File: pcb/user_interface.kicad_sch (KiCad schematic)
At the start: 8 parts, among them SW3 GSPTS0018

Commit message: Finished user interface
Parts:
- added D5: B38G3RGB, B38G3RGB:B38G3RGB-10D0003H2U1930_HVK, symbol Device:LED_RGBA
- added Q6: NTR4003N, Package_TO_SOT_SMD:SOT-23-3, symbol Transistor_FET:Q_NMOS_GSD
- added R34: 430, Resistor_SMD:R_0603_1608Metric, symbol Device:R_Small_US
- added R35, R36: 330, Resistor_SMD:R_0603_1608Metric, symbol Device:R_Small_US
- added R37: 100, symbol Device:R_Small_US
- added R38: 47k, symbol Device:R_Small_US
- added SW4, SW5, SW6: GSPTS0018, PTS815_SJM_250_SMTR_LFS:SW_Push_PTS815_SJM_250_SMTR_LFS, symbol Switch:SW_Push
- R17: value 330 -> 430
- R32, R33: value 150 -> 330
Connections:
- net +3V3: now also BZ1.1 (+), D4.1 (K), SW3.2, SW4.2, SW5.2, SW6.2
- net +BATT: now also D5.4 (A)
- net BTN_0: now also SW3.1
- net BTN_1: now also SW4.1
- net BTN_2: now also SW5.1
- net BTN_3: now also SW6.1
- net MODE_1: now also S1.1
- net MODE_2: now also S1.2
- net MODE_4: now also S1.4
- net MODE_C: now also S1.C
- net at BZ1.2 (-): now also D4.2 (A), Q6.3 (D)
- new net: Q6.1 (G), R37.2, R38.1
- new net: D5.2 (GK), R35.1
- new net: D5.1 (RK), R34.1
- new net: D5.3 (BK), R36.1
- new net BUZZER: R37.1
- new net GND: Q6.2 (S), R38.2
- new net LED1_B: R36.2
- new net LED1_G: R35.2
- new net LED1_R: R34.2
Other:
- note added: "15 mA"
- note added: "red 2V green/blue 3.3V"
- note removed: "red 2V green/blue 3V"
- moved on the sheet: BZ1, D4

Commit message: Start layout
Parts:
- D4: footprint (none) -> Diode_SMD:D_SMA
- R33: renamed from R37; footprint (none) -> Resistor_SMD:R_0603_1608Metric
- R35: renamed from R38; footprint (none) -> Resistor_SMD:R_0603_1608Metric
- renumbered R17 to R32, R32 to R34, R33 to R36, R34 to R37, R35 to R38, R36 to R39
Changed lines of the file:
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@@
 		(on_board yes)
 		(dnp no)
-		(property "Reference" "R32"
+		(property "Reference" "R34"
 			(at 45.212 44.45 0)
 			(effects
@@
 			(project "airbrake_mod"
 				(path "/1f4fd4ed-9886-4375-a5ac-dc32d5760936/0a32b07f-7988-40ae-8006-b298a5ae2a50"
-					(reference "R32")
+					(reference "R34")
 					(unit 1)
 				)
@@
 		(dnp no)
 		(fields_autoplaced yes)
-		(property "Reference" "#PWR077"
+		(property "Reference" "#PWR067"
 			(at 158.75 80.01 0)
 			(effects
@@
 			(project "airbrake_mod"
 				(path "/1f4fd4ed-9886-4375-a5ac-dc32d5760936/0a32b07f-7988-40ae-8006-b298a5ae2a50"
-					(reference "#PWR077")
+					(reference "#PWR067")
 					(unit 1)
 				)
@@
 			)
 		)
-		(property "Footprint" ""
+		(property "Footprint" "Diode_SMD:D_SMA"
 			(at 60.96 133.35 90)
 			(effects
@@
 		(dnp no)
 		(fields_autoplaced yes)
-		(property "Reference" "#PWR081"
+		(property "Reference" "#PWR062"
 			(at 63.5 171.45 0)
 			(effects
@@
 			(project "airbrake_mod"
 				(path "/1f4fd4ed-9886-4375-a5ac-dc32d5760936/0a32b07f-7988-40ae-8006-b298a5ae2a50"
-					(reference "#PWR081")
+					(reference "#PWR062")
 					(unit 1)
 				)
@@
 		(dnp no)
 		(fields_autoplaced yes)
-		(property "Reference" "#PWR069"
+		(property "Reference" "#PWR061"
 			(at 63.5 130.81 0)
 			(effects
@@
 			(project ""
 				(path "/1f4fd4ed-9886-4375-a5ac-dc32d5760936/0a32b07f-7988-40ae-8006-b298a5ae2a50"
-					(reference "#PWR069")
+					(reference "#PWR061")
 					(unit 1)
 				)
@@
 		(dnp no)
 		(fields_autoplaced yes)
-		(property "Reference" "R38"
+		(property "Reference" "R35"
 			(at 53.34 157.4799 0)
 			(effects
@@
 			)
 		)
-		(property "Footprint" ""
+		(property "Footprint" "Resistor_SMD:R_0603_1608Metric"
 			(at 50.8 158.75 0)
 			(effects
@@
 			(project "airbrake_mod"
 				(path "/1f4fd4ed-9886-4375-a5ac-dc32d5760936/0a32b07f-7988-40ae-8006-b298a5ae2a50"
-					(reference "R38")
+					(reference "R35")
 					(unit 1)
 				)
@@
 		(dnp no)
 		(fields_autoplaced yes)
-		(property "Reference" "#PWR080"
+		(property "Reference" "#PWR060"
 			(at 50.8 171.45 0)
 			(effects
@@
 			(project "airbrake_mod"
 				(path "/1f4fd4ed-9886-4375-a5ac-dc32d5760936/0a32b07f-7988-40ae-8006-b298a5ae2a50"
-					(reference "#PWR080")
+					(reference "#PWR060")
 					(unit 1)
 				)
@@
 		(dnp no)
 		(fields_autoplaced yes)
-		(property "Reference" "#PWR075"
+		(property "Reference" "#PWR064"
 			(at 120.65 80.01 0)
 			(effects
@@
 			(project "airbrake_mod"
 				(path "/1f4fd4ed-9886-4375-a5ac-dc32d5760936/0a32b07f-7988-40ae-8006-b298a5ae2a50"
-					(reference "#PWR075")
+					(reference "#PWR064")
 					(unit 1)
 				)
@@
 		(on_board yes)
 		(dnp no)
-		(property "Reference" "R35"
+		(property "Reference" "R38"
 			(at 121.412 44.45 0)
 			(effects
@@
 			(project "airbrake_mod"
 				(path "/1f4fd4ed-9886-4375-a5ac-dc32d5760936/0a32b07f-7988-40ae-8006-b298a5ae2a50"
-					(reference "R35")
+					(reference "R38")
 					(unit 1)
 				)
@@
 		(dnp no)
 		(fields_autoplaced yes)
-		(property "Reference" "#PWR076"
+		(property "Reference" "#PWR066"
 			(at 139.7 80.01 0)
 			(effects
@@
 			(project "airbrake_mod"
 				(path "/1f4fd4ed-9886-4375-a5ac-dc32d5760936/0a32b07f-7988-40ae-8006-b298a5ae2a50"
-					(reference "#PWR076")
+					(reference "#PWR066")
 					(unit 1)
 				)
@@
 		(on_board yes)
 		(dnp no)
-		(property "Reference" "R34"
+		(property "Reference" "R37"
 			(at 108.712 44.45 0)
 			(effects
@@
 			(project "airbrake_mod"
 				(path "/1f4fd4ed-9886-4375-a5ac-dc32d5760936/0a32b07f-7988-40ae-8006-b298a5ae2a50"
-					(reference "R34")
+					(reference "R37")
 					(unit 1)
 				)
@@
 		(on_board yes)
 		(dnp no)
-		(property "Reference" "R36"
+		(property "Reference" "R39"
 			(at 134.112 44.45 0)
 			(effects
@@
 			(project "airbrake_mod"
 				(path "/1f4fd4ed-9886-4375-a5ac-dc32d5760936/0a32b07f-7988-40ae-8006-b298a5ae2a50"
-					(reference "R36")
+					(reference "R39")
 					(unit 1)
 				)
@@
 		(dnp no)
 		(fields_autoplaced yes)
-		(property "Reference" "R37"
+		(property "Reference" "R33"
 			(at 44.45 146.05 90)
 			(effects
@@
 			)
 		)
-		(property "Footprint" ""
+		(property "Footprint" "Resistor_SMD:R_0603_1608Metric"
 			(at 44.45 152.4 0)
 			(effects
@@
 			(project "airbrake_mod"
 				(path "/1f4fd4ed-9886-4375-a5ac-dc32d5760936/0a32b07f-7988-40ae-8006-b298a5ae2a50"
-					(reference "R37")
+					(reference "R33")
 					(unit 1)
 				)
@@
 		(dnp no)
 		(fields_autoplaced yes)
-		(property "Reference" "#PWR052"
+		(property "Reference" "#PWR059"
 			(at 50.8 29.21 0)
 			(effects
@@
 			(project "airbrake_mod"
 				(path "/1f4fd4ed-9886-4375-a5ac-dc32d5760936/0a32b07f-7988-40ae-8006-b298a5ae2a50"
-					(reference "#PWR052")
+					(reference "#PWR059")
 					(unit 1)
 				)
@@
 		(dnp no)
 		(fields_autoplaced yes)
-		(property "Reference" "#PWR074"
+		(property "Reference" "#PWR063"
 			(at 101.6 80.01 0)
 			(effects
@@
 			(project ""
 				(path "/1f4fd4ed-9886-4375-a5ac-dc32d5760936/0a32b07f-7988-40ae-8006-b298a5ae2a50"
-					(reference "#PWR074")
+					(reference "#PWR063")
 					(unit 1)
 				)
@@
 		(dnp no)
 		(fields_autoplaced yes)
-		(property "Reference" "#PWR078"
+		(property "Reference" "#PWR065"
 			(at 127 29.21 0)
 			(effects
@@
 			(project "airbrake_mod"
 				(path "/1f4fd4ed-9886-4375-a5ac-dc32d5760936/0a32b07f-7988-40ae-8006-b298a5ae2a50"
-					(reference "#PWR078")
+					(reference "#PWR065")
 					(unit 1)
 				)
@@
 		(on_board yes)
 		(dnp no)
-		(property "Reference" "R17"
+		(property "Reference" "R32"
 			(at 32.512 44.45 0)
 			(effects
@@
 			(project "airbrake_mod"
 				(path "/1f4fd4ed-9886-4375-a5ac-dc32d5760936/0a32b07f-7988-40ae-8006-b298a5ae2a50"
-					(reference "R17")
+					(reference "R32")
 					(unit 1)
 				)
@@
 		(on_board yes)
 		(dnp no)
-		(property "Reference" "R33"
+		(property "Reference" "R36"
 			(at 57.912 44.45 0)
 			(effects
@@
 			(project "airbrake_mod"
 				(path "/1f4fd4ed-9886-4375-a5ac-dc32d5760936/0a32b07f-7988-40ae-8006-b298a5ae2a50"
-					(reference "R33")
-					(unit 1)
-				)
+					(reference "R36")
+					(unit 1)
+				)

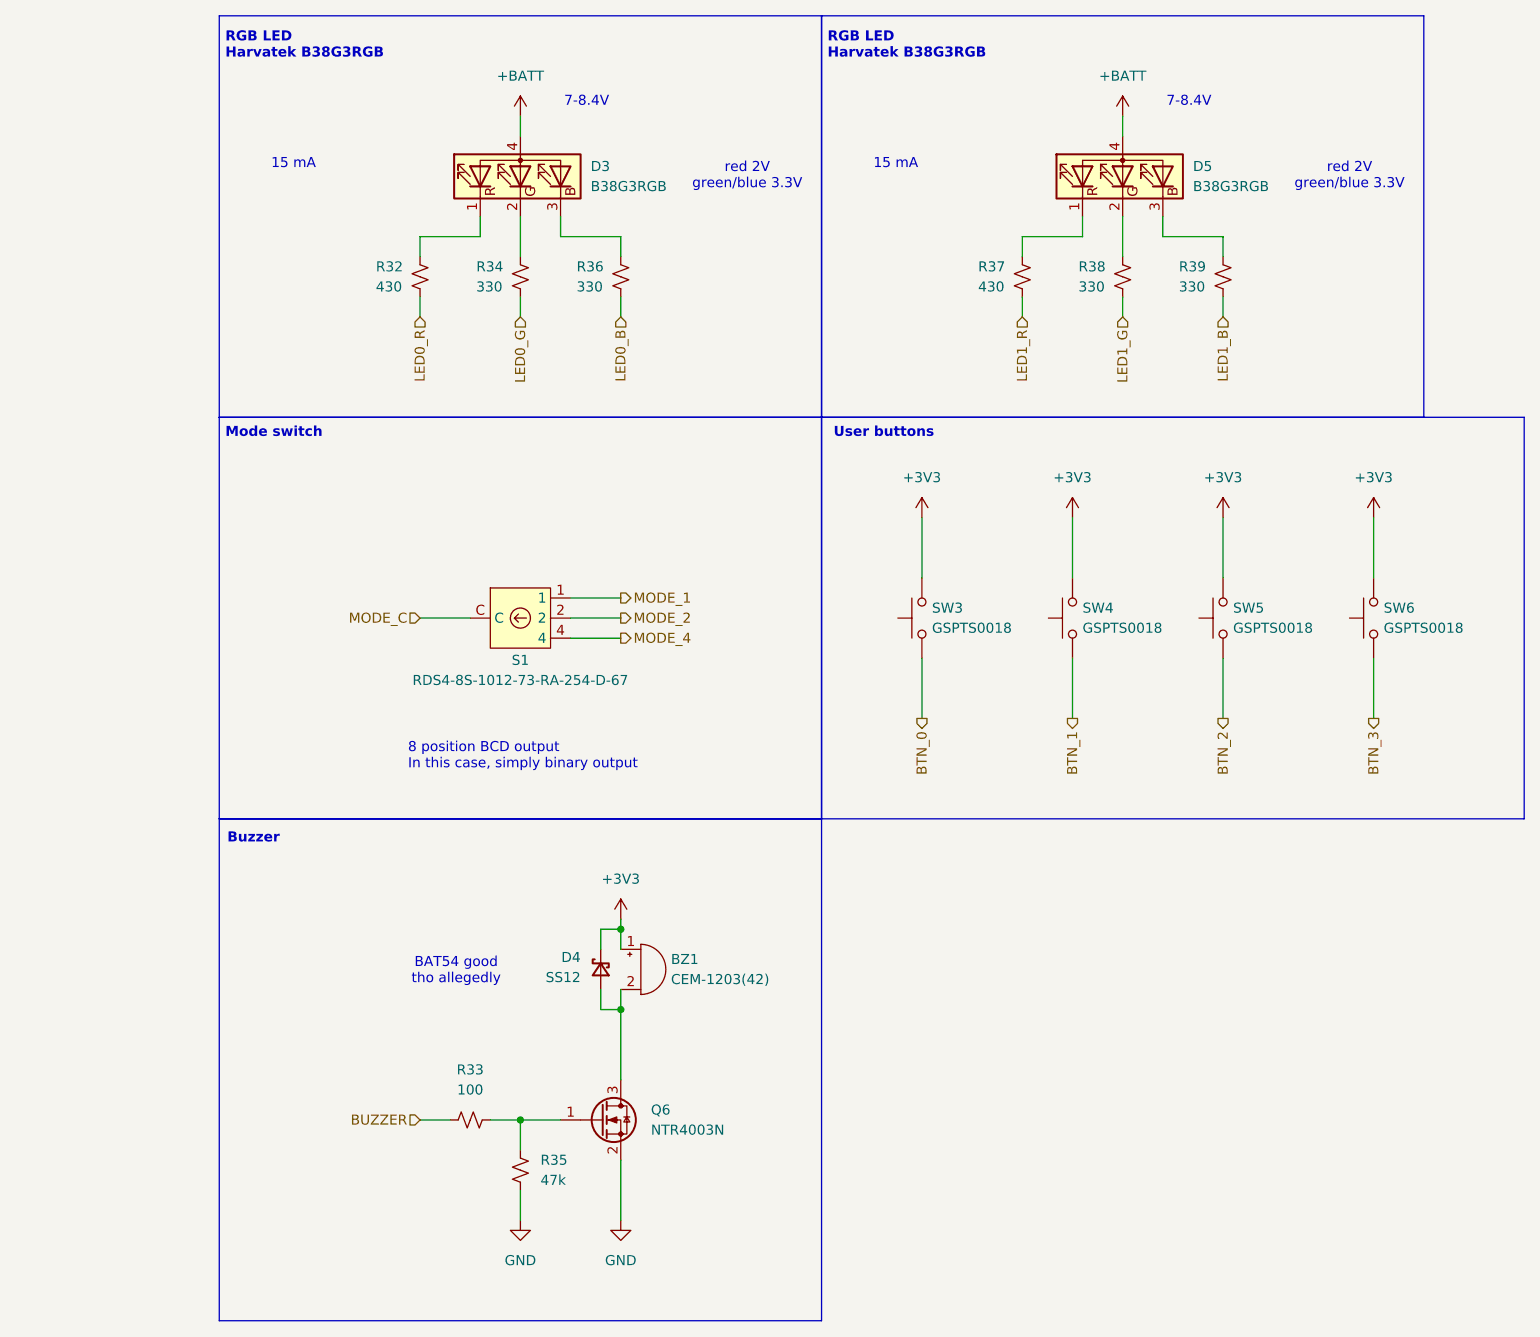
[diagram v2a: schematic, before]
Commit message: Layout MCU decoupling
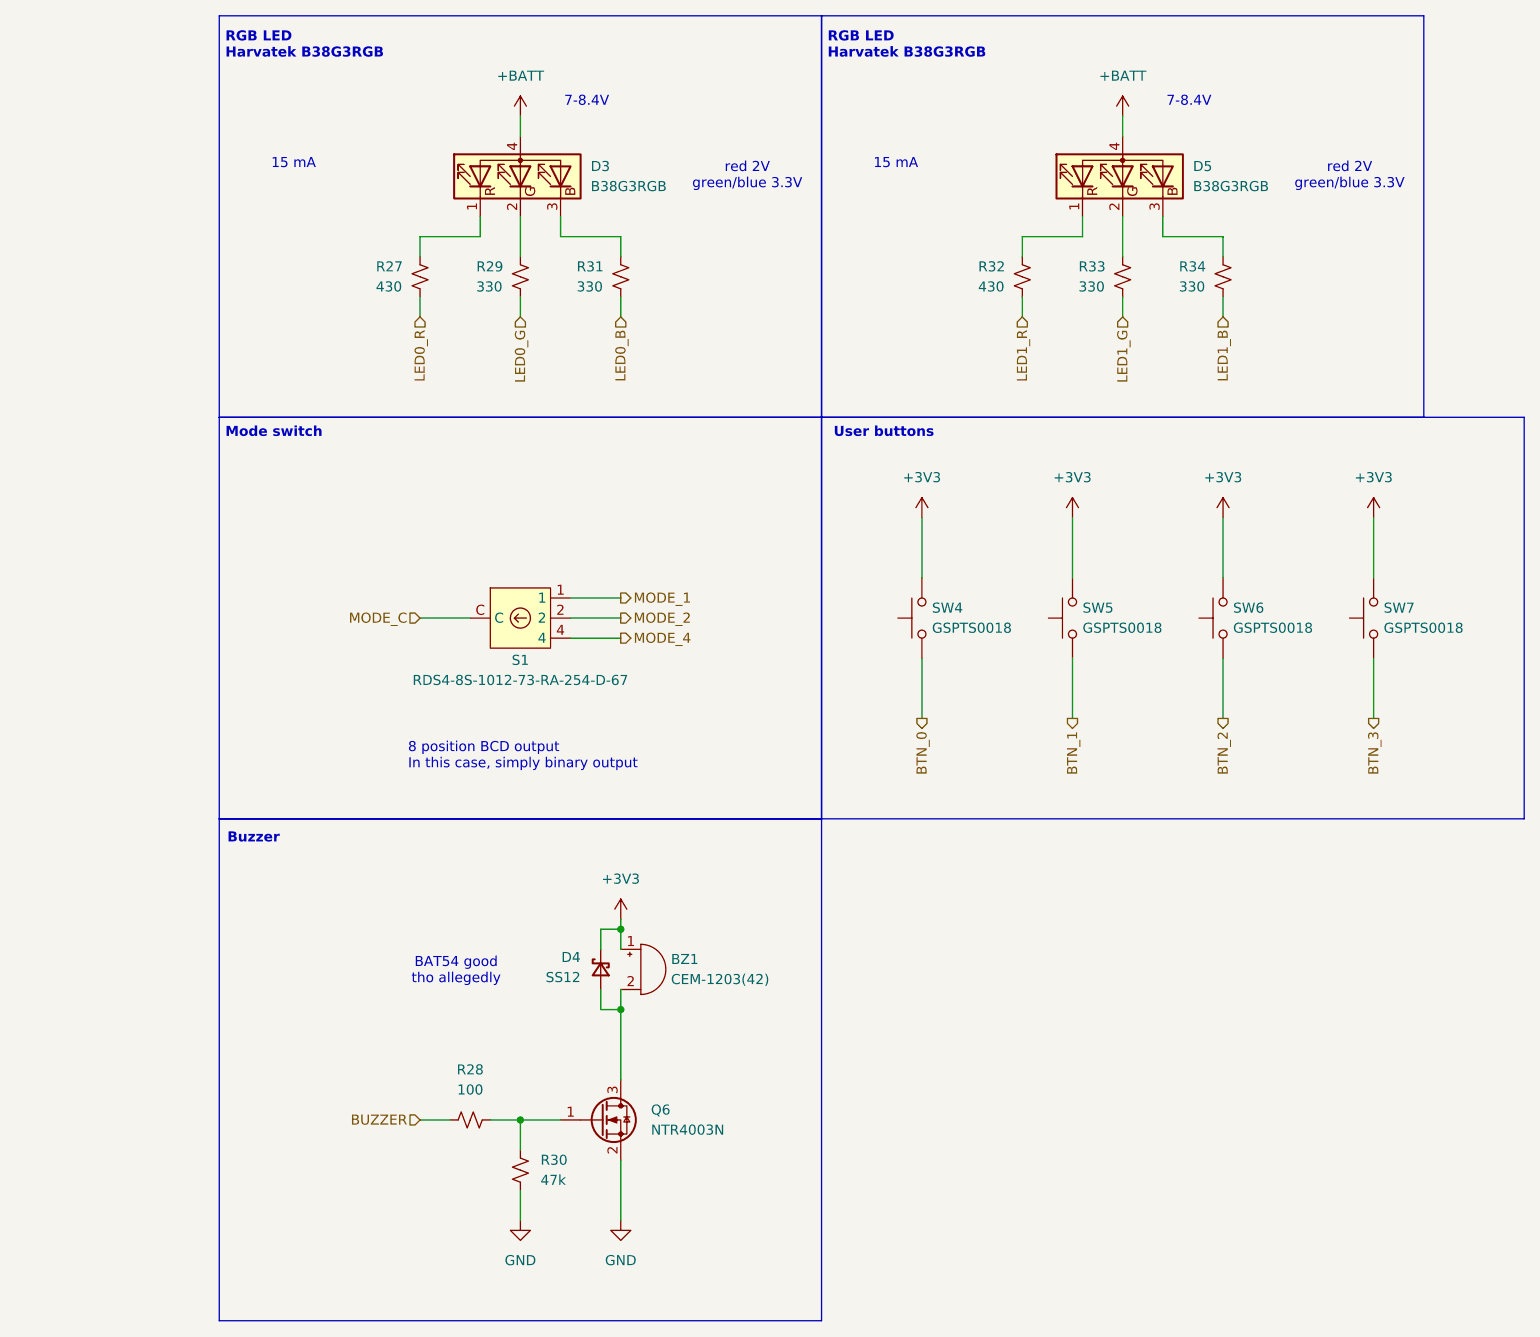
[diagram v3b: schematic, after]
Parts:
- renumbered R32 to R27, R33 to R28, R34 to R29, R35 to R30, R36 to R31, R37 to R32, R38 to R33, R39 to R34, SW3 to SW4, SW4 to SW5, SW5 to SW6, SW6 to SW7
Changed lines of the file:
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@@
 		(on_board yes)
 		(dnp no)
-		(property "Reference" "R34"
+		(property "Reference" "R29"
 			(at 45.212 44.45 0)
 			(effects
@@
 			(project "airbrake_mod"
 				(path "/1f4fd4ed-9886-4375-a5ac-dc32d5760936/0a32b07f-7988-40ae-8006-b298a5ae2a50"
-					(reference "R34")
+					(reference "R29")
 					(unit 1)
 				)
@@
 		(dnp no)
 		(fields_autoplaced yes)
-		(property "Reference" "SW3"
+		(property "Reference" "SW4"
 			(at 102.87 87.6299 90)
 			(effects
@@
 			(project ""
 				(path "/1f4fd4ed-9886-4375-a5ac-dc32d5760936/0a32b07f-7988-40ae-8006-b298a5ae2a50"
-					(reference "SW3")
+					(reference "SW4")
 					(unit 1)
 				)
@@
 		(dnp no)
 		(fields_autoplaced yes)
-		(property "Reference" "R35"
+		(property "Reference" "R30"
 			(at 53.34 157.4799 0)
 			(effects
@@
 			(project "airbrake_mod"
 				(path "/1f4fd4ed-9886-4375-a5ac-dc32d5760936/0a32b07f-7988-40ae-8006-b298a5ae2a50"
-					(reference "R35")
+					(reference "R30")
 					(unit 1)
 				)
@@
 		(dnp no)
 		(fields_autoplaced yes)
-		(property "Reference" "SW6"
+		(property "Reference" "SW7"
 			(at 160.02 87.6299 90)
 			(effects
@@
 			(project "airbrake_mod"
 				(path "/1f4fd4ed-9886-4375-a5ac-dc32d5760936/0a32b07f-7988-40ae-8006-b298a5ae2a50"
-					(reference "SW6")
+					(reference "SW7")
 					(unit 1)
 				)
@@
 		(on_board yes)
 		(dnp no)
-		(property "Reference" "R38"
+		(property "Reference" "R33"
 			(at 121.412 44.45 0)
 			(effects
@@
 			(project "airbrake_mod"
 				(path "/1f4fd4ed-9886-4375-a5ac-dc32d5760936/0a32b07f-7988-40ae-8006-b298a5ae2a50"
-					(reference "R38")
+					(reference "R33")
 					(unit 1)
 				)
@@
 		(on_board yes)
 		(dnp no)
-		(property "Reference" "R37"
+		(property "Reference" "R32"
 			(at 108.712 44.45 0)
 			(effects
@@
 			(project "airbrake_mod"
 				(path "/1f4fd4ed-9886-4375-a5ac-dc32d5760936/0a32b07f-7988-40ae-8006-b298a5ae2a50"
-					(reference "R37")
+					(reference "R32")
 					(unit 1)
 				)
@@
 		(on_board yes)
 		(dnp no)
-		(property "Reference" "R39"
+		(property "Reference" "R34"
 			(at 134.112 44.45 0)
 			(effects
@@
 			(project "airbrake_mod"
 				(path "/1f4fd4ed-9886-4375-a5ac-dc32d5760936/0a32b07f-7988-40ae-8006-b298a5ae2a50"
-					(reference "R39")
+					(reference "R34")
 					(unit 1)
 				)
@@
 		(dnp no)
 		(fields_autoplaced yes)
-		(property "Reference" "SW5"
+		(property "Reference" "SW6"
 			(at 140.97 87.6299 90)
 			(effects
@@
 			(project "airbrake_mod"
 				(path "/1f4fd4ed-9886-4375-a5ac-dc32d5760936/0a32b07f-7988-40ae-8006-b298a5ae2a50"
-					(reference "SW5")
+					(reference "SW6")
 					(unit 1)
 				)
@@
 		(dnp no)
 		(fields_autoplaced yes)
-		(property "Reference" "SW4"
+		(property "Reference" "SW5"
 			(at 121.92 87.6299 90)
 			(effects
@@
 			(project "airbrake_mod"
 				(path "/1f4fd4ed-9886-4375-a5ac-dc32d5760936/0a32b07f-7988-40ae-8006-b298a5ae2a50"
-					(reference "SW4")
+					(reference "SW5")
 					(unit 1)
 				)
@@
 		(dnp no)
 		(fields_autoplaced yes)
-		(property "Reference" "R33"
+		(property "Reference" "R28"
 			(at 44.45 146.05 90)
 			(effects
@@
 			(project "airbrake_mod"
 				(path "/1f4fd4ed-9886-4375-a5ac-dc32d5760936/0a32b07f-7988-40ae-8006-b298a5ae2a50"
-					(reference "R33")
+					(reference "R28")
 					(unit 1)
 				)
@@
 		(on_board yes)
 		(dnp no)
-		(property "Reference" "R32"
+		(property "Reference" "R27"
 			(at 32.512 44.45 0)
 			(effects
@@
 			(project "airbrake_mod"
 				(path "/1f4fd4ed-9886-4375-a5ac-dc32d5760936/0a32b07f-7988-40ae-8006-b298a5ae2a50"
-					(reference "R32")
+					(reference "R27")
 					(unit 1)
 				)
@@
 		(on_board yes)
 		(dnp no)
-		(property "Reference" "R36"
+		(property "Reference" "R31"
 			(at 57.912 44.45 0)
 			(effects
@@
 			(project "airbrake_mod"
 				(path "/1f4fd4ed-9886-4375-a5ac-dc32d5760936/0a32b07f-7988-40ae-8006-b298a5ae2a50"
-					(reference "R36")
-					(unit 1)
-				)
+					(reference "R31")
+					(unit 1)
+				)
